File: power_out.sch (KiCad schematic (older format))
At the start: 4 parts

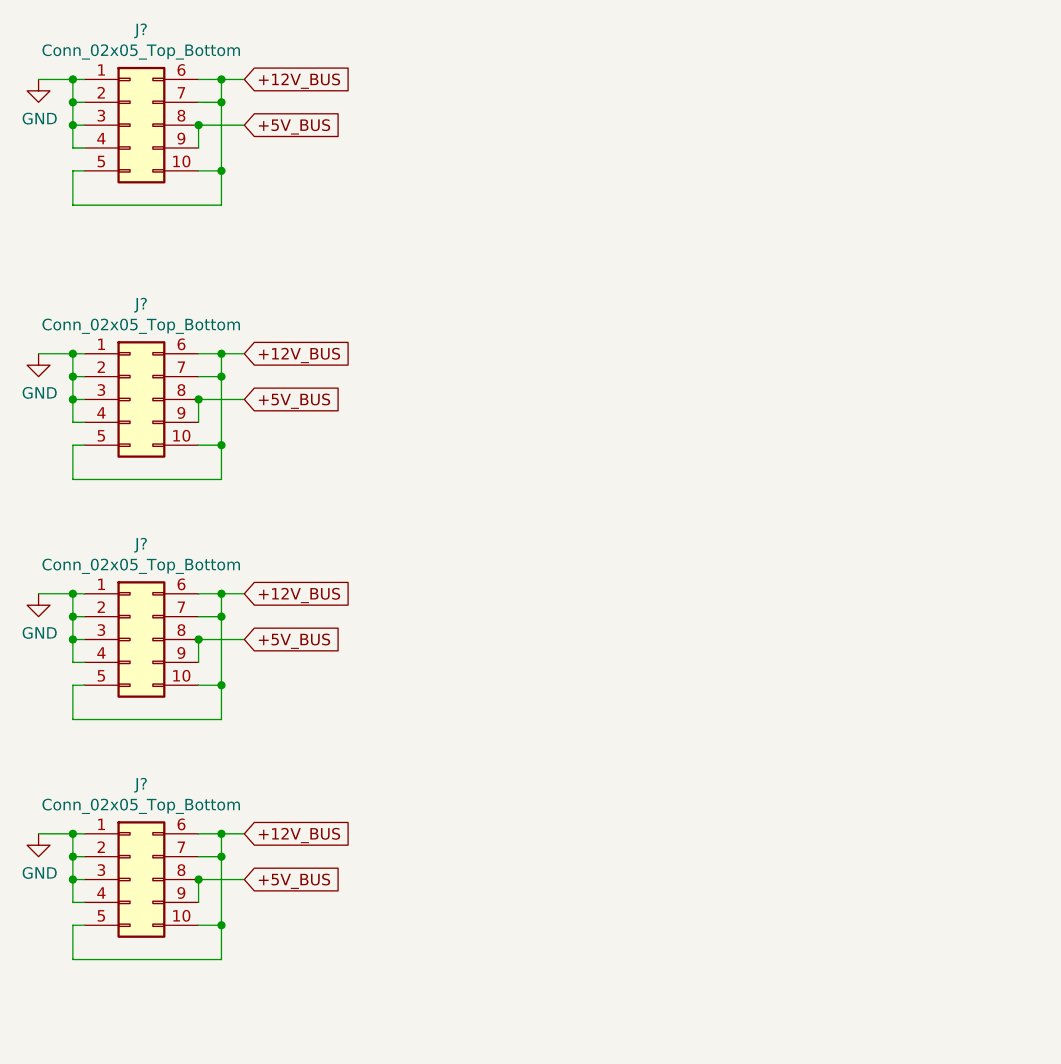
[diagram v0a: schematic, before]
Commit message: add some capacitor in fan and power_out
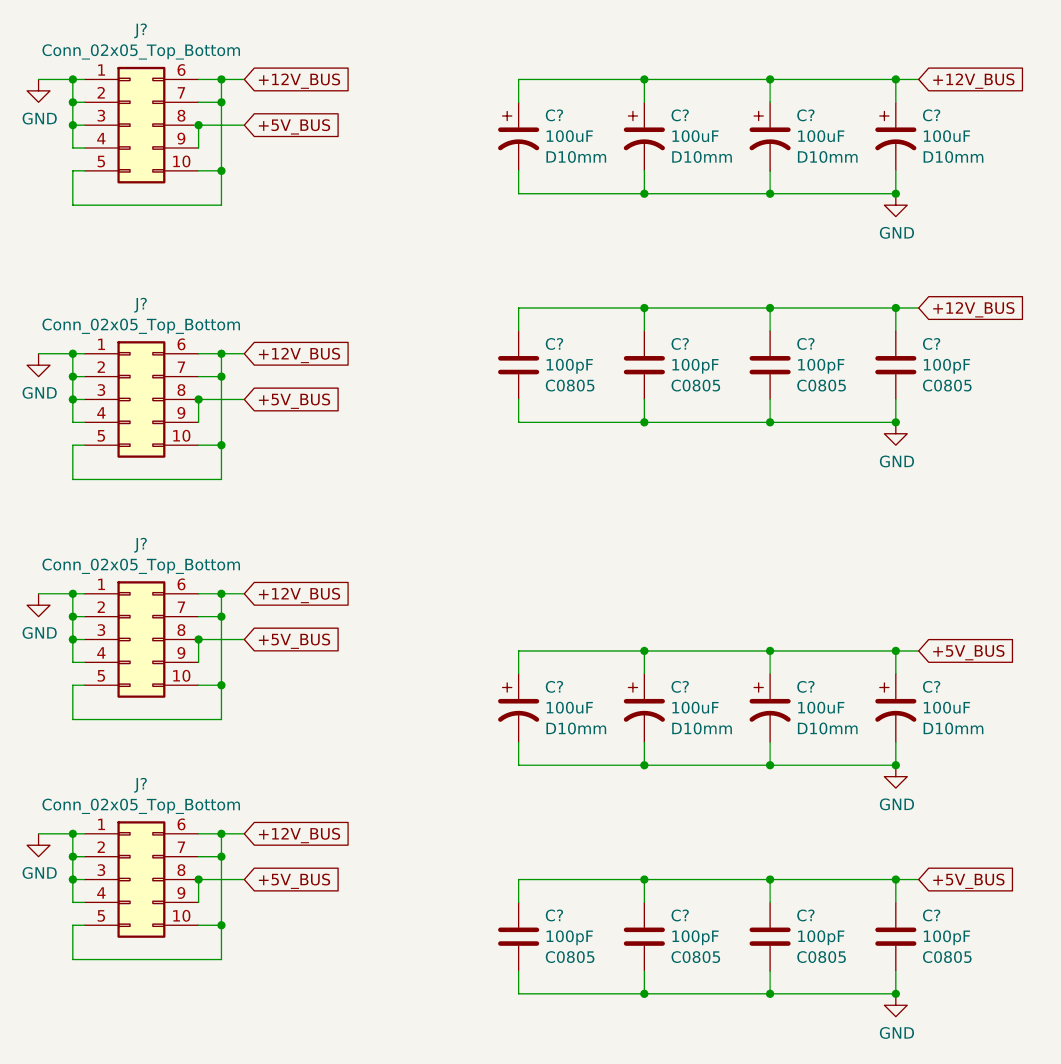
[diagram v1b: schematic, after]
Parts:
- added C? (x8): 100uF, Capacitor_THT:CP_Radial_D10.0mm_P2.50mm_P5.00mm, symbol Device:CP1
- added C? (x8): 100pF, Capacitor_SMD:C_0805_2012Metric, symbol Device:C
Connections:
- net +12V_BUS: now also C?.1, C?.1, C?.1, C?.1, C?.1, C?.1, C?.1, C?.1
- net +5V_BUS: now also C?.1, C?.1, C?.1, C?.1, C?.1, C?.1, C?.1, C?.1
- net GND: now also C?.2, C?.2, C?.2, C?.2, C?.2, C?.2, C?.2, C?.2, C?.2, C?.2, C?.2, C?.2, C?.2, C?.2, C?.2, C?.2
